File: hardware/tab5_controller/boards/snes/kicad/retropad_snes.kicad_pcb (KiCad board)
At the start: 2 copper layers, 125 x 55 mm, 46 parts, among them J1 Tab5 Ext.Port1, J2 SWD, SW1 UP, SW10 START, SW11 MENU, SW12 L, SW13 R, SW2 DOWN, SW3 LEFT, SW4 RIGHT, SW5 X, SW6 B, SW7 Y, SW8 A, SW9 SELECT, U1 STM32F030C8T6

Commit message: tab5_controller: build every console board on the AVR32DD28
The STM32F030 matrix boards are gone. SNES, NES, Game Boy, Genesis and
Master System / Game Gear are now all AVR32DD28 boards: one MCU pin per
button, no diodes, UPDI programming, one firmware image (firmware_avrdd)
keyed by the console-ID straps.

- layout.py / gen_pcb.py / gen_sch.py: drop the stm32 core (LQFP-48,
  key matrix, diodes, SWD header, AN_EN strap); the AVR DD core is the
  only one, and the *_dd board names become the plain console names.
- SNES, NES and Genesis keep the routing of their AVR DD prototypes;
  Game Boy and Master System are routed fresh.
- Every board: DRC 0 unconnected (silkscreen warnings only), schematic
  vs PCB 0 differences, and each switch checked against the MCU pin
  pinmap.h gives it for that console ID.
- Host test now also covers the Game Boy and Master System pin maps.
- READMEs describe the AVR DD boards only.

Co-Authored-By: Claude Opus 5.5 <noreply@anthropic.com>
Claude-Session: https://claude.ai/code/session_01NhSHTsezreiVZCnuBhQzP2
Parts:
- removed C5: 100nF, Capacitor_SMD:C_0603_1608Metric
- removed D1, D10, D11, D12, D13, D2, D3, D4, D5, D6, D7, D8, D9: 1N4148W, Diode_SMD:D_SOD-123
- removed R10: DNP, Resistor_SMD:R_0603_1608Metric
- removed R4, R5: 10k, Resistor_SMD:R_0603_1608Metric
- added R11: DNP, Resistor_SMD:R_0603_1608Metric, B.Cu at (76.0, 93.0)
- J2: value SWD -> UPDI; footprint Connector_PinHeader_2.54mm:PinHeader_1x05_P2.54mm_Vertical -> Connector_PinHeader_2.54mm:PinHeader_1x03_P2.54mm_Vertical
- U1: value STM32F030C8T6 -> AVR32DD28-I/SO; footprint Package_QFP:LQFP-48_7x7mm_P0.5mm -> Package_SO:SOIC-28W_7.5x17.9mm_P1.27mm
- moved R3 17.2 mm to (97.6, 85.7)
- moved C4 12.7 mm to (116.0, 90.5), turned to 90 degrees
- moved C2 11.5 mm to (102.1, 85.7)
- moved C3 7.98 mm to (106.0, 101.6), turned to 180 degrees
- moved C1 5.83 mm to (92.0, 96.0)
- moved J2 2.00 mm to (130.0, 86.5)
- moved R6 2.00 mm to (121.0, 99.0)
- moved R7 2.00 mm to (124.0, 99.0)
- moved R8 2.00 mm to (127.0, 99.0)
- moved R9 2.00 mm to (130.0, 99.0)
- moved U1 0.50 mm to (104.0, 93.5), turned to 90 degrees
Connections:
- J1 pad 10: (no net) -> G9_UPDI
- J1 pad 9: INT -> (no net)
- J2 pad 2: SWCLK -> UPDI
- J2 pad 3: SWDIO -> GND
- R3 pad 2: INT -> RESET
- SW1 pad 2: COL0 -> GND
- SW10 pad 2: COL1 -> GND
- SW11 pad 2: COL2 -> GND
- SW12 pad 2: COL1 -> GND
- SW13 pad 2: COL1 -> GND
- SW2 pad 2: COL0 -> GND
- SW3 pad 2: COL0 -> GND
- SW4 pad 2: COL0 -> GND
- SW5 pad 2: COL0 -> GND
- SW6 pad 2: COL0 -> GND
- SW7 pad 2: COL1 -> GND
- SW8 pad 2: COL0 -> GND
- SW9 pad 2: COL1 -> GND
- U1 pad 1: +3V3 -> ID3
- U1 pad 10: COL0 -> K_RIGHT
- U1 pad 11: COL1 -> K_X
- U1 pad 12: COL2 -> K_B
- U1 pad 13: COL3 -> K_Y
- U1 pad 14: (no net) -> +3V3
- U1 pad 15: (no net) -> GND
- U1 pad 16: (no net) -> K_L
- U1 pad 17: (no net) -> K_R
- U1 pad 18: ROW0 -> RESET
- U1 pad 19: ROW1 -> UPDI
- U1 pad 2: (no net) -> K_A
- U1 pad 20: ROW2 -> +3V3
- U1 pad 21: SCL -> GND
- U1 pad 22: SDA -> ID0
- U1 pad 23: GND -> ID1
- U1 pad 24: +3V3 -> SDA
- U1 pad 25: ID0 -> SCL
- U1 pad 26: ID1 -> AN0
- U1 pad 27: ID2 -> AN1
- U1 pad 28: (no net) -> ID2
- U1 pad 3: (no net) -> K_SELECT
- U1 pad 4: (no net) -> K_START
- U1 pad 5: (no net) -> K_MENU
- U1 pad 6: (no net) -> +3V3
- U1 pad 7: NRST -> K_UP
- U1 pad 8: GND -> K_DOWN
- U1 pad 9: +3V3 -> K_LEFT
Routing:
- net GND: track 131.3 -> 360.7 mm, vias 2 -> 0
- net COL0: track 215.7 -> 0.00 mm
- net COL1: track 169.7 -> 0.00 mm
- net ROW3: track 99.0 -> 0.00 mm, vias 2 -> 0
- net ROW0: track 96.0 -> 0.00 mm
- net ROW1: track 75.2 -> 0.00 mm
- net ROW2: track 69.8 -> 0.00 mm
- net ROW4: track 68.4 -> 0.00 mm
- net ROW7: track 68.1 -> 0.00 mm, vias 3 -> 0
- net K_R: track 9.53 -> 70.7 mm, vias 0 -> 1
- net UPDI: track 0.00 -> 59.8 mm, vias 0 -> 1
- net ROW5: track 58.2 -> 0.00 mm, vias 2 -> 0
- net NRST: track 55.3 -> 0.00 mm, vias 1 -> 0
- net K_L: track 8.16 -> 60.2 mm, vias 0 -> 1
- net K_B: track 15.9 -> 61.1 mm, vias 0 -> 1
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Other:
- board text added: "ID0 ID1 ID2 ID3"
- board text added: "UPDI 3V3 UPDI GND"
- board text removed: "ID0 ID1 ID2 ID3 AN"
- board text removed: "SWD 3V3 CLK DIO RST GND"

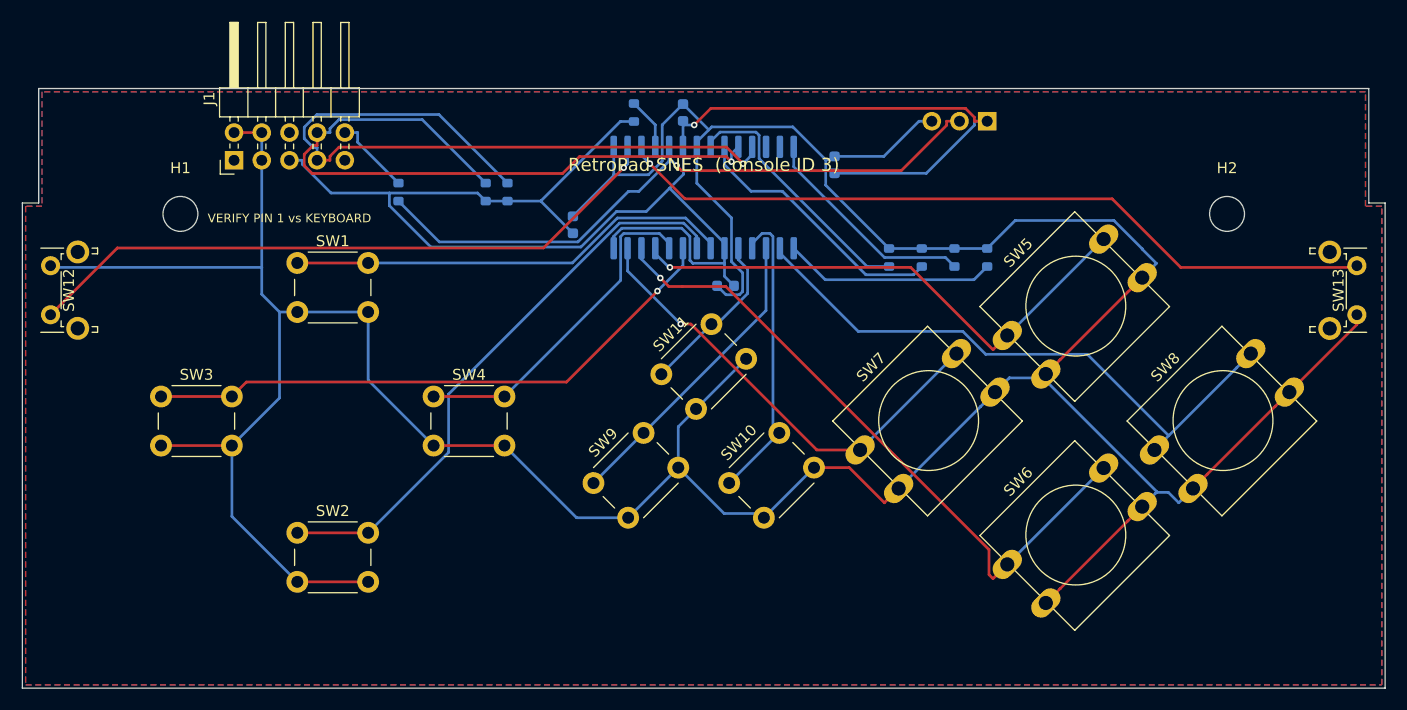
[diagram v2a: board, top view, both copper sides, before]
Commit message: tab5_controller: remove the UPDI-to-G9 link (R11) from every board
The Tab5 never updates controller firmware, so J1 pin 10 (G9) is left
unconnected, as on M5Stack's keyboard, and R11 and the G9_UPDI net are
gone. Boards are programmed only through their own UPDI header J2.

All five boards are re-routed (the old routes ended at R11). Game Boy
is routed with Freerouting 2.1 single-threaded because 1.9 stalls with
UPDI unrouted on it. Every board: DRC 0 unconnected pads (silkscreen
warnings only), schematic vs PCB 0 differences, switches on the pins
pinmap.h expects.

Co-Authored-By: Claude Opus 5.5 <noreply@anthropic.com>
Claude-Session: https://claude.ai/code/session_01NhSHTsezreiVZCnuBhQzP2
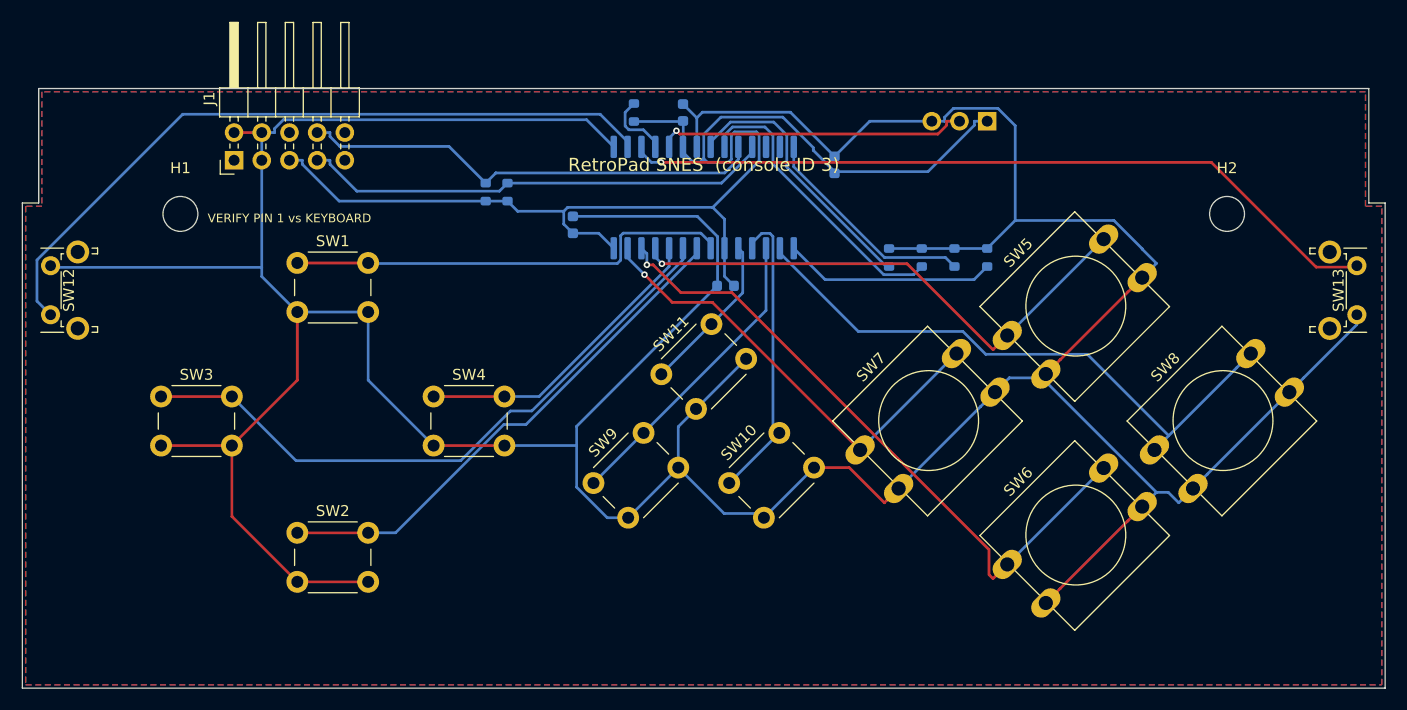
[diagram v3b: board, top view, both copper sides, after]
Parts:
- removed R11: DNP, Resistor_SMD:R_0603_1608Metric
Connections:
- J1 pad 10: G9_UPDI -> (no net)
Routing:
- net GND: track 360.7 -> 406.2 mm
- net +3V3: track 149.0 -> 115.2 mm, vias 1 -> 0
- net UPDI: track 59.8 -> 28.5 mm
- net SCL: track 67.8 -> 43.3 mm, vias 1 -> 0
- net SDA: track 64.3 -> 42.8 mm, vias 1 -> 0
- net G9_UPDI: track 7.36 -> 0.00 mm
- net K_L: track 60.2 -> 66.8 mm, vias 1 -> 0
- net K_DOWN: track 53.1 -> 47.7 mm
- net K_LEFT: track 54.4 -> 59.0 mm, vias 1 -> 0
- net K_RIGHT: track 31.0 -> 28.2 mm
- net ID1: track 24.2 -> 27.0 mm
- net RESET: track 4.78 -> 6.24 mm
- net ID0: track 23.6 -> 24.8 mm
- net K_Y: track 42.7 -> 42.0 mm
- net K_MENU: track 15.5 -> 14.8 mm

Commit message: tab5_controller: 0805 hand-solder passives on every board
Swap the 0603 resistors and capacitors (decoupling, I2C pull-ups, reset
pull-up, console-ID straps) for KiCad's 0805 HandSolder footprints, which
have longer pads for soldering by hand. C2 turns 90 degrees so its larger
courtyard clears U1. All four boards are re-routed with Freerouting 1.9;
schematics, BOMs, DRC reports and renders are regenerated.

DRC: 0 errors and 0 unconnected pads on every board (silkscreen and
library-path warnings only). Schematic vs PCB: 0 differences.

Co-Authored-By: Claude Opus 5.5 <noreply@anthropic.com>
Claude-Session: https://claude.ai/code/session_016pgTnJvu7Wh4anaUwDfFmN
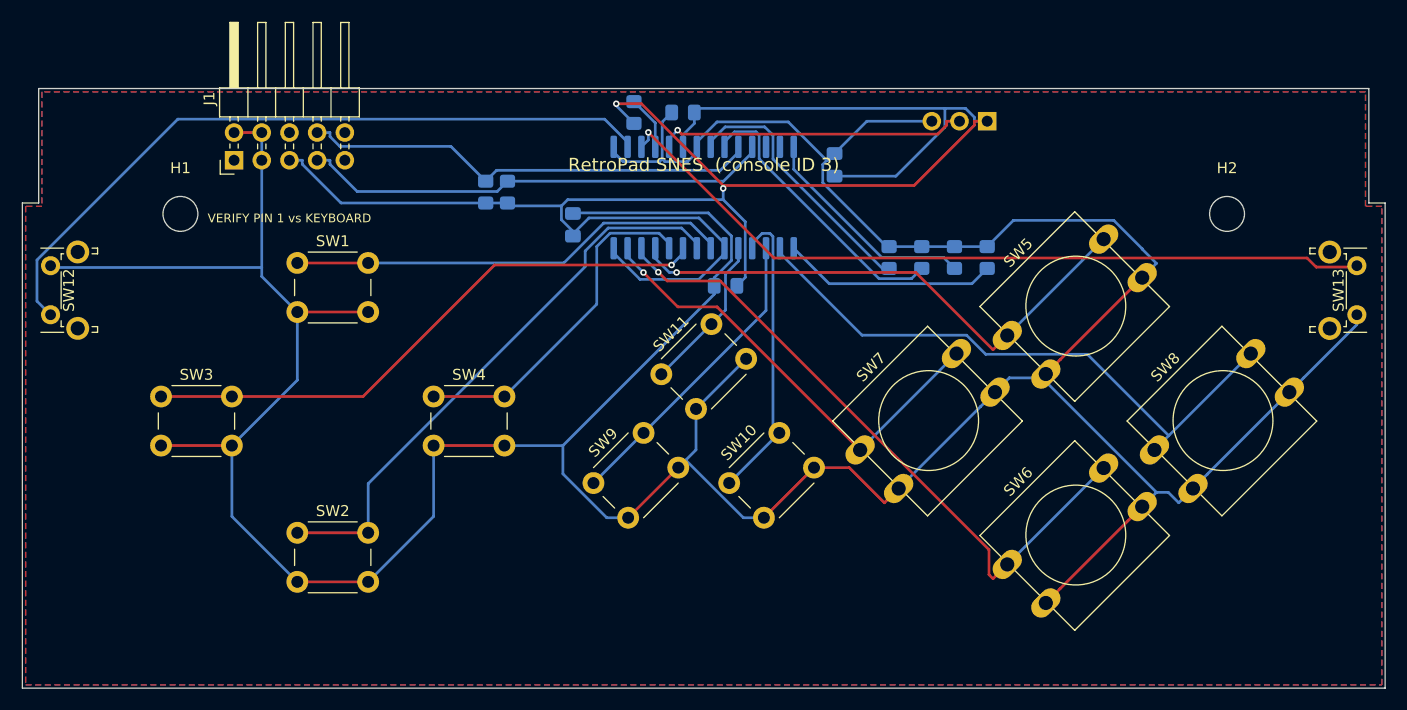
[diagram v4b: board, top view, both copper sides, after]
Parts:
- C1, C2, C3, C4: footprint Capacitor_SMD:C_0603_1608Metric -> Capacitor_SMD:C_0805_2012Metric_Pad1.18x1.45mm_HandSolder
- R1, R2, R3, R6, R7, R8, R9: footprint Resistor_SMD:R_0603_1608Metric -> Resistor_SMD:R_0805_2012Metric_Pad1.20x1.40mm_HandSolder
- turned C2 to 180 degrees
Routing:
- net +3V3: track 115.2 -> 171.7 mm, vias 0 -> 2
- net GND: track 406.2 -> 377.3 mm
- net K_LEFT: track 59.0 -> 53.8 mm, vias 0 -> 1
- net K_DOWN: track 47.7 -> 52.7 mm
- net K_RIGHT: track 28.2 -> 31.7 mm
- net RESET: track 6.24 -> 4.96 mm
- net K_R: track 70.5 -> 71.8 mm
- net ID1: track 27.0 -> 26.2 mm
- net ID0: track 24.8 -> 24.1 mm
- net K_UP: track 41.3 -> 40.7 mm
- net SDA: track 42.8 -> 42.3 mm

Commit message: tab5_controller: 4-pin tact switch symbols and footprints
The 6x6 and 12x12 switches are 4-leg parts, and the production layout in
EasyEDA uses their 4-pin symbols, so the KiCad boards now match:

- kicad_lib/RetroPad.pretty: SW_PUSH_6mm_4pin and SW_PUSH-12mm_4pin,
  KiCad's footprints with the pads renumbered 1-4 (pad 1 top-left, then
  clockwise; tied pairs 1-2 and 3-4, the legs 6.5 / 12.5 mm apart).
  gen_pcb.py writes them from the stock footprints and points each
  board's fp-lib-table at the library.
- RetroPad:SW_Push_4pin symbol in gen_sch.py: 1-2 tied, 4-3 tied, one
  contact between. KiCad's 4-pin SW_Push_Dual is a two-contact switch,
  so it doesn't fit these parts.
- Wiring: legs 1-2 to GND, 3-4 to K_<button>. L/R (right angle, two
  contacts plus mounting legs) keep the 2-pin SW_Push.
- All four boards re-routed: DRC 0 unconnected (silkscreen warnings
  only), schematic vs PCB 0 differences, every switch on the pin
  pinmap.h expects; firmware host test passes; Gerber/drill export OK.

Co-Authored-By: Claude Opus 5.5 <noreply@anthropic.com>
Claude-Session: https://claude.ai/code/session_01NhSHTsezreiVZCnuBhQzP2
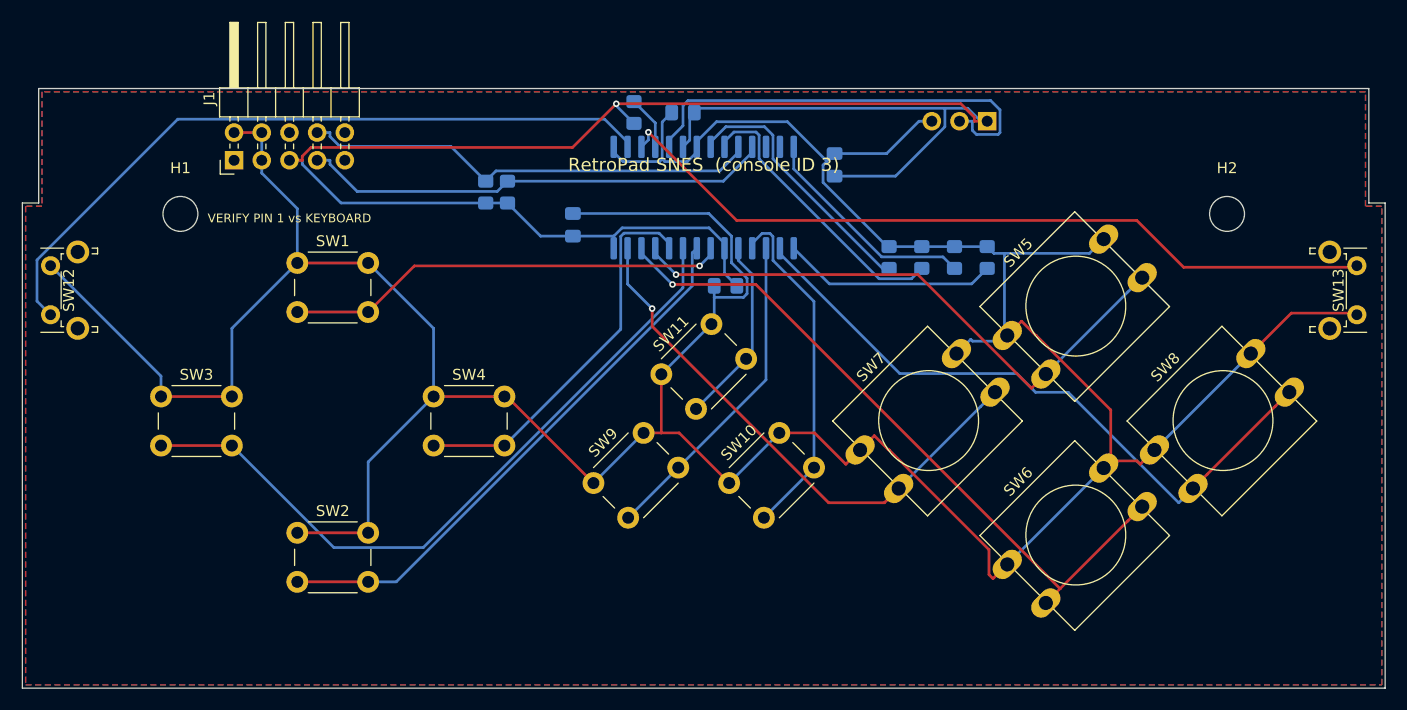
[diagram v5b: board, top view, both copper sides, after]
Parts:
- SW1, SW10, SW11, SW2, SW3, SW4, SW9: footprint Button_Switch_THT:SW_PUSH_6mm -> RetroPad:SW_PUSH_6mm_4pin
- SW5, SW6, SW7, SW8: footprint Button_Switch_THT:SW_PUSH-12mm -> RetroPad:SW_PUSH-12mm_4pin
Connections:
- SW1 pad 1: K_UP -> GND
- SW10 pad 1: K_START -> GND
- SW11 pad 1: K_MENU -> GND
- SW2 pad 1: K_DOWN -> GND
- SW3 pad 1: K_LEFT -> GND
- SW4 pad 1: K_RIGHT -> GND
- SW5 pad 1: K_X -> GND
- SW6 pad 1: K_B -> GND
- SW7 pad 1: K_Y -> GND
- SW8 pad 1: K_A -> GND
- SW9 pad 1: K_SELECT -> GND
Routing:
- net GND: track 377.3 -> 351.5 mm
- net UPDI: track 28.6 -> 40.8 mm, vias 1 -> 0
- net K_LEFT: track 53.8 -> 65.3 mm, vias 1 -> 0
- net K_Y: track 41.9 -> 50.4 mm
- net +3V3: track 171.7 -> 163.9 mm, vias 2 -> 1
- net K_A: track 55.5 -> 60.9 mm
- net K_X: track 49.7 -> 54.5 mm
- net K_START: track 27.6 -> 32.1 mm
- net K_RIGHT: track 31.7 -> 35.5 mm
- net K_B: track 60.9 -> 64.1 mm
- net K_MENU: track 14.5 -> 17.4 mm
- net K_SELECT: track 28.1 -> 30.0 mm
- net K_DOWN: track 52.7 -> 51.1 mm
- net K_UP: vias 0 -> 1

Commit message: tab5_controller: label each console-ID strap under its own resistor
The back silkscreen printed one mirrored "ID0 ID1 ID2 ID3" string, which
reads left to right from the back while the straps appear right to left
(R9/ID3 first), so the labels were in the reverse order of the parts.
Each strap now gets its own ID<n> label centred under it. Silkscreen
only: the boards keep their routing (same segments and vias), DRC 0
unconnected, schematic vs PCB 0 differences.

Co-Authored-By: Claude Opus 5.5 <noreply@anthropic.com>
Claude-Session: https://claude.ai/code/session_01NhSHTsezreiVZCnuBhQzP2
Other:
- board text added: "ID0"
- board text added: "ID1"
- board text added: "ID2"
- board text added: "ID3"
- board text removed: "ID0 ID1 ID2 ID3"
